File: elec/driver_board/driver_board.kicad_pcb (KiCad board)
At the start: 2 copper layers, 226.2 x 90.5 mm, 131 parts, among them J1 rotary_encoder, J2 DCF77 board, J3 RTC, M1 Conn motor 0, M10 Conn motor 1, M11 Conn motor 0, M12 Conn motor 1, M13 Conn motor 0, M14 Conn motor 1, M15 Conn motor 0, M16 Conn motor 1, M17 Conn motor 0, M18 Conn motor 1, M19 Conn motor 0, M2 Conn motor 1, M20 Conn motor 1, M21 Conn motor 0, M22 Conn motor 1, M23 Conn motor 0, M24 Conn motor 1, M3 Conn motor 0, M4 Conn motor 1, M5 Conn motor 0, M6 Conn motor 1, M7 Conn motor 0, M8 Conn motor 1, M9 Conn motor 0, U1 ESP32-C3-DEVKITM-1, U10 VID6606, U11 74HCT595, U12 VID6606, U13 74HCT595, U14 VID6606, U15 74HCT595, U16 VID6606, U17 74HCT595, U18 VID6606, U19 74HCT595, U2 TXB0102DCT, U20 VID6606, U21 74HCT595, U22 VID6606, U23 74HCT595, U24 VID6606, U25 74HCT595, U26 VID6606, U3 74HCT595, U4 VID6606, U5 74HCT595, U6 VID6606, U7 74HCT595, U8 VID6606, U9 74HCT595

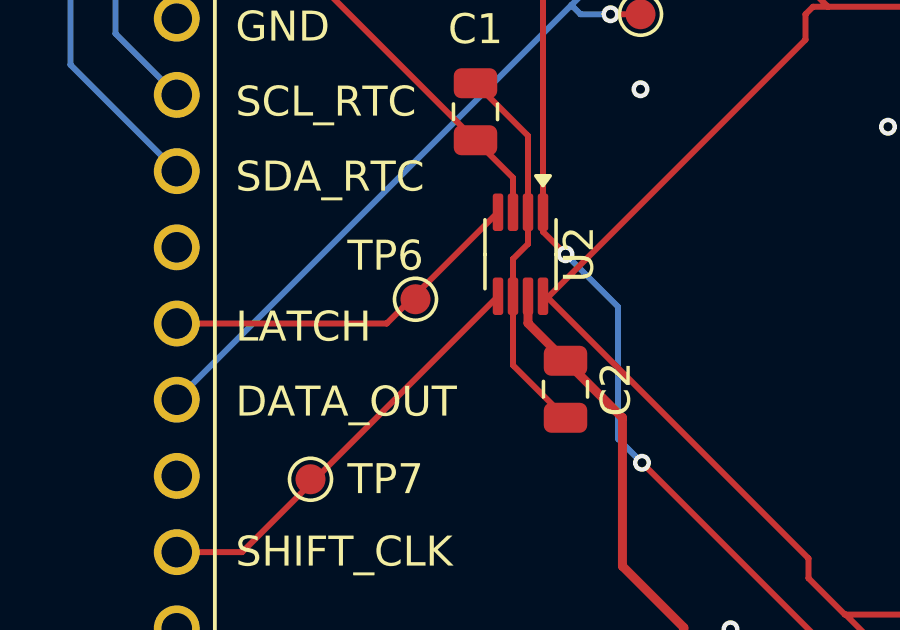
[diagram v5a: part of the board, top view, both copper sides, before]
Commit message: Fix OE for the level shifter
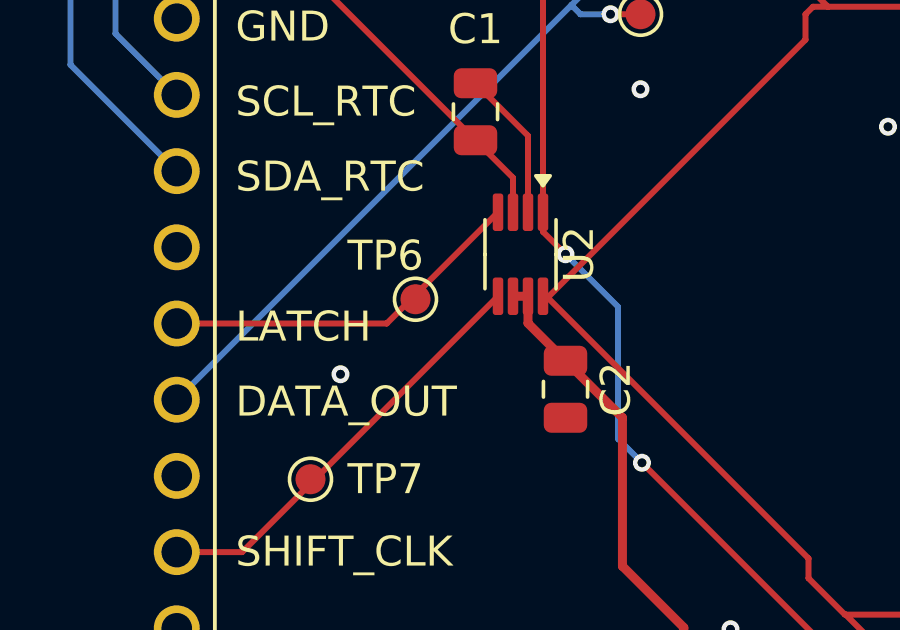
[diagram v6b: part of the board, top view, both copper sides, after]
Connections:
- U2 pad 6: GND -> VCC
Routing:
- net GND: track 14.5 -> 6.68 mm, vias 138 -> 139
- net VCC: track 1231.4 -> 1231.9 mm
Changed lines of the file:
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@@
 			(layers "F.Cu" "F.Mask" "F.Paste")
 			(roundrect_rratio 0.25)
-			(net 1 "GND")
+			(net 5 "VCC")
 			(pinfunction "OE")
 			(pintype "input")
@@
 	)
 	(segment
-		(start 92.75 84.4)
-		(end 92.75 83.157358)
-		(width 0.2)
-		(layer "F.Cu")
-		(net 1)
-	)
-	(segment
-		(start 92.75 83.157358)
-		(end 93.25 82.657358)
-		(width 0.2)
-		(layer "F.Cu")
-		(net 1)
-	)
-	(segment
 		(start 93.25 79.05)
 		(end 91.5 77.3)
@@
 	)
 	(segment
-		(start 92.75 86.7)
-		(end 94.5 88.45)
-		(width 0.2)
-		(layer "F.Cu")
-		(net 1)
-	)
-	(segment
 		(start 93.25 81.6)
 		(end 93.25 79.05)
@@
 		(net 1)
 	)
-	(segment
-		(start 93.25 82.657358)
-		(end 93.25 81.6)
-		(width 0.2)
-		(layer "F.Cu")
-		(net 1)
-	)
-	(segment
-		(start 92.75 84.4)
-		(end 92.75 86.7)
-		(width 0.2)
-		(layer "F.Cu")
-		(net 1)
-	)
 	(via
 		(at 209.75 84.5)
@@
 	)
 	(via
+		(at 87 87)
+		(size 0.6)
+		(drill 0.3)
+		(layers "F.Cu" "B.Cu")
+		(free yes)
+		(net 1)
+	)
+	(via
 		(at 106.5 110)
 		(size 0.6)
@@
 		(width 0.3)
 		(layer "F.Cu")
+		(net 5)
+	)
+	(segment
+		(start 92.75 84.4)
+		(end 93.25 84.4)
+		(width 0.3)
+		(layer "F.Cu")
